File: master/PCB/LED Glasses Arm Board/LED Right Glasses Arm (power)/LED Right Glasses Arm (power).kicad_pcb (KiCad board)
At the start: 2 copper layers, 130.8 x 20.4 mm, 26 parts, among them J1 PWR IN, J2 PWR OUT +, J3 PWR OUT -, Q1 TP0610T, SW1 EN, U1 TPS63061DSCT

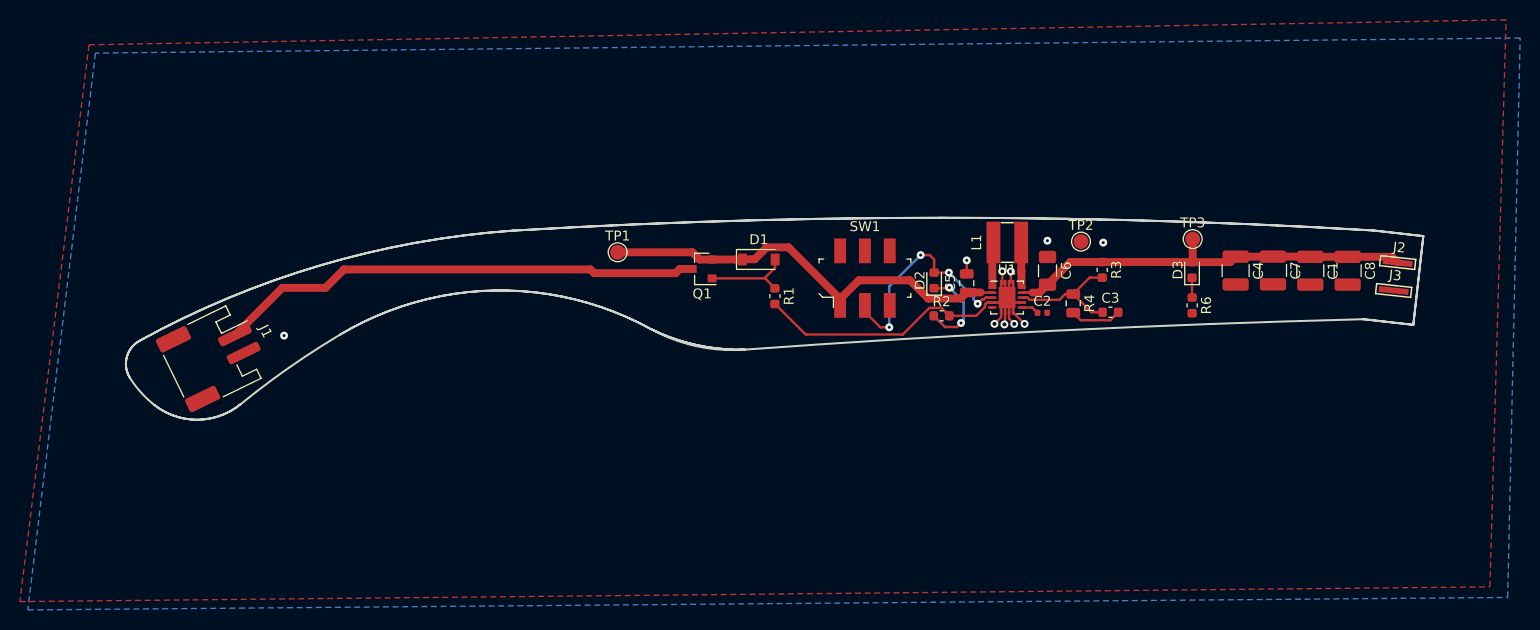
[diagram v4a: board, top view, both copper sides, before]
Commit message: Changed LED indicator from 5V out to PG from power reg IC, moved annotation from 0-x to 100-1xx to keep it consistent with mcu arm design, adjusted layout to accomodate schematic changes from this commit and the previous and added silkscreen labels to input and output.
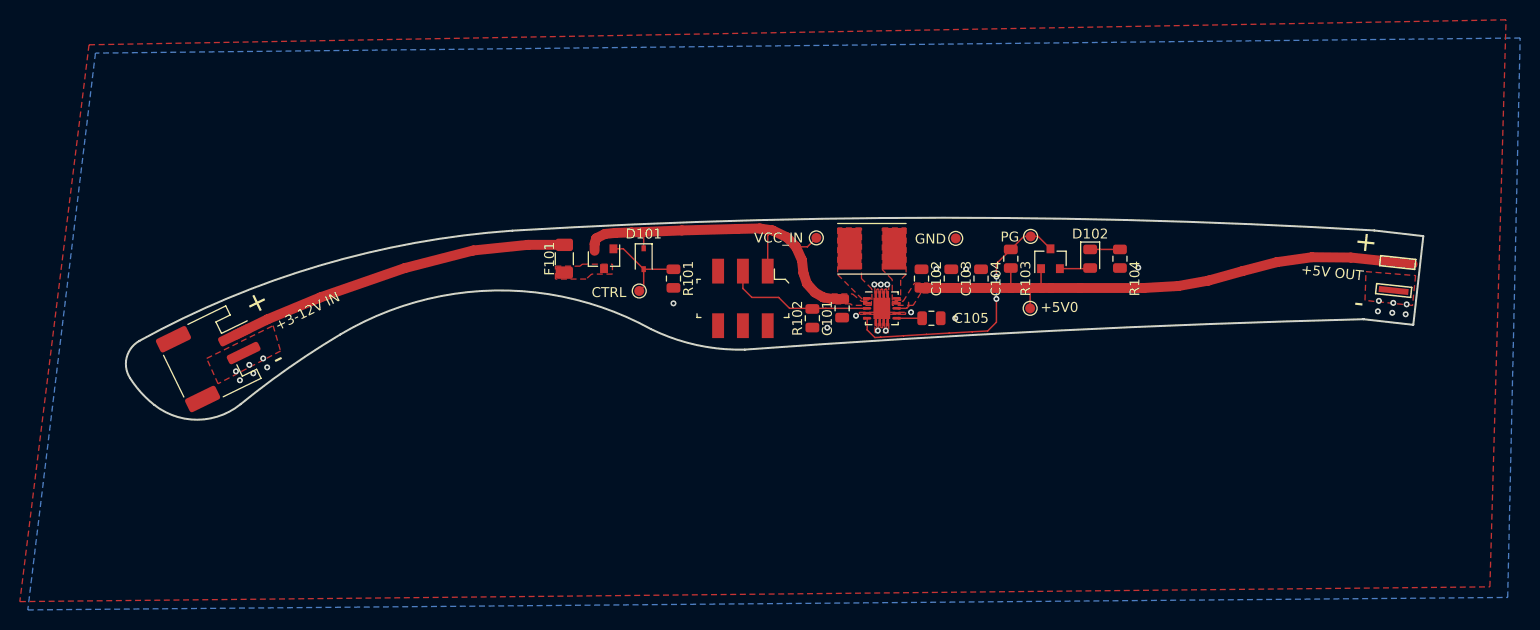
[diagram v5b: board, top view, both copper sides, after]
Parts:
- removed C1, C4, C7, C8: 220u, Capacitor_SMD:C_1210_3225Metric
- removed C2: 0.1u, Capacitor_SMD:C_0402_1005Metric
- removed C3: 10p, Capacitor_SMD:C_0603_1608Metric
- removed C5: 22u, Capacitor_SMD:C_0805_2012Metric
- removed C6: 68u, Capacitor_SMD:C_1206_3216Metric
- removed D1: 6V, Diode_SMD:D_SOD-123
- removed D2: P_IN, LED_SMD:LED_0603_1608Metric
- removed D3: P_OUT, LED_SMD:LED_0603_1608Metric
- removed J1: PWR IN, Connector_JST:JST_PH_S2B-PH-SM4-TB_1x02-1MP_P2.00mm_Horizontal
- removed L1: 1u, sft:SRN4018TA
- removed Q1: TP0610T, Package_TO_SOT_SMD:SOT-23
- removed R1: 100k1, Resistor_SMD:R_0603_1608Metric
- removed R2, R6: 2k2, Resistor_SMD:R_0603_1608Metric
- removed R3: 1M, Resistor_SMD:R_0603_1608Metric
- removed R4: 111k, Resistor_SMD:R_0805_2012Metric
- removed TP1: VIN, TestPoint:TestPoint_Pad_D1.5mm
- removed TP2: GND, TestPoint:TestPoint_Pad_D1.5mm
- removed TP3: VOUT, TestPoint:TestPoint_Pad_D1.5mm
- removed U1: TPS63061DSCT, Package_SON:Texas_S-PWSON-N10
- added C101: 22U_25V, Capacitor_SMD:C_0805_2012Metric, F.Cu at (158.0, 98.0)
- added C102: 22U_25V, Capacitor_SMD:C_0805_2012Metric, F.Cu at (166.0, 95.0)
- added C103: 22U_25V, Capacitor_SMD:C_0805_2012Metric, F.Cu at (169.0, 95.0)
- added C104: 22U_25V, Capacitor_SMD:C_0805_2012Metric, F.Cu at (172.0, 95.0)
- added C105: 100N_15V, Capacitor_SMD:C_0805_2012Metric, F.Cu at (167.0, 99.0)
- added D101: D_TVS, Diode_SMD:D_SOD-323, F.Cu at (138.0, 93.0)
- added D102: P_GOOD, LED_SMD:LED_0805_2012Metric, F.Cu at (183.0, 93.0)
- added F101: FUSE 2A, Resistor_SMD:R_1206_3216Metric, F.Cu at (130.0, 93.0)
- added J101: PWR_IN, Connector_JST:JST_PH_S2B-PH-SM4-TB_1x02-1MP_P2.00mm_Horizontal, F.Cu at (94.7, 102.9)
- added L101: 1U, Inductor_SMD:L_Taiyo-Yuden_NR-50xx_HandSoldering, F.Cu at (161.0, 92.0)
- added Q101: TP0610T, Package_TO_SOT_SMD:SOT-23, F.Cu at (134.0, 93.0)
- added Q102: TP0610T, Package_TO_SOT_SMD:SOT-23, F.Cu at (179.0, 93.0)
- added R101: 100K, Resistor_SMD:R_0805_2012Metric, F.Cu at (141.0, 95.0)
- added R102: 100K, Resistor_SMD:R_0805_2012Metric, F.Cu at (155.0, 99.0)
- added R103: 1M, Resistor_SMD:R_0805_2012Metric, F.Cu at (175.0, 93.0)
- added R104: 270, Resistor_SMD:R_0805_2012Metric, F.Cu at (186.0, 93.0)
- added TP101: TP_GND, TestPoint:TestPoint_Pad_D1.0mm, F.Cu at (169.4, 91.0)
- added TP102: TP_5V0, TestPoint:TestPoint_Pad_D1.0mm, F.Cu at (176.9, 98.0)
- added TP103: TP_IN_SAFE, TestPoint:TestPoint_Pad_D1.0mm, F.Cu at (155.4, 90.9)
- added TP104: TP_PG, TestPoint:TestPoint_Pad_D1.0mm, F.Cu at (177.0, 90.8)
- added TP105: TP_POL, TestPoint:TestPoint_Pad_D1.0mm, F.Cu at (137.6, 96.2)
- added U101: TPS63061DSCT, Package_SON:Texas_S-PWSON-N10, F.Cu at (162.0, 98.0)
- J102: renamed from J2; value PWR OUT + -> PWR_OUT_P
- J103: renamed from J3; value PWR OUT - -> PWR_OUT_N
- moved SW101 12.5 mm to (148.0, 97.0), turned to 180 degrees
- renumbered SW1 to SW101
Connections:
- J102 pad 1: /VOUT_5V -> +5V
- SW101 pad 1: Net-(C5-Pad1) -> /VCC_IN_SAFE
- SW101 pad 2: Net-(D2-Pad2) -> /EN
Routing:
- net +5V: track 0.00 -> 57.6 mm
- net /VIN_2.5-12V: track 49.2 -> 0.00 mm
- net GND: track 44.7 -> 0.00 mm, vias 10 -> 25
- net Net-(C5-Pad1): track 43.2 -> 0.00 mm
- net /VOUT_5V: track 42.0 -> 0.00 mm
- net /VCC_IN_SAFE: track 0.00 -> 38.2 mm
- net /VCC_IN: track 0.00 -> 34.8 mm
- net /PG: track 0.00 -> 27.9 mm, vias 0 -> 2
- net Net-(D2-Pad2): track 22.8 -> 0.00 mm, vias 4 -> 0
- net /EN: track 0.00 -> 15.1 mm
- net Net-(C3-Pad1): track 12.9 -> 0.00 mm
- net /POL_MOS_CTRL: track 0.00 -> 9.29 mm
- net Net-(D2-Pad1): track 9.22 -> 0.00 mm, vias 2 -> 0
- net Net-(D1-Pad2): track 9.10 -> 0.00 mm
- net Net-(L1-Pad1): track 4.35 -> 0.00 mm
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- added copper zone on F.Cu, net +5V
- added copper zone on F.Cu, net /L1
- added copper zone on F.Cu, net /L2
- added copper zone on F.Cu, net /VCC_IN_FUSED
- added copper zone on F.Cu, net /VCC_IN_SAFE
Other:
- outline, holes or cut-outs redrawn
- net class Default: clearance 0.2 -> 0.15; trace_width 0.25 -> 0.15; via_dia 0.8 -> 0.6
- rule trace_clearance: 0.2 -> 0.15
- rule trace_min: 0.2 -> 0.15
- rule via_min_size: 0.4 -> 0.6
- board text added: "+"
- board text added: "+3-12V IN"
- board text added: "+5V OUT"
- board text added: "+5V0"
- board text added: "-"
- board text added: "CTRL"
- board text added: "GND"
- board text added: "PG"
- board text added: "VCC_IN"
